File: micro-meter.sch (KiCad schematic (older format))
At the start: 105 parts, among them U1 XC6206P332MR, U2 STM32F411CEU6

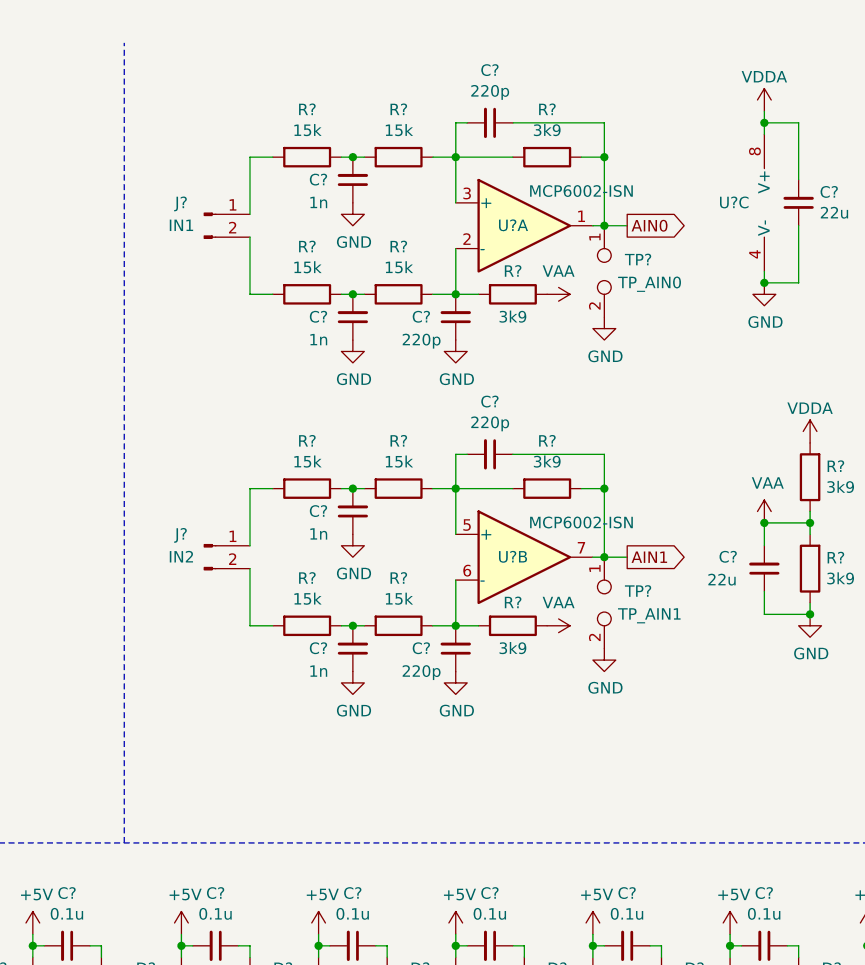
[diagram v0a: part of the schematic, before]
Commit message: Add MFB anti-alias filters
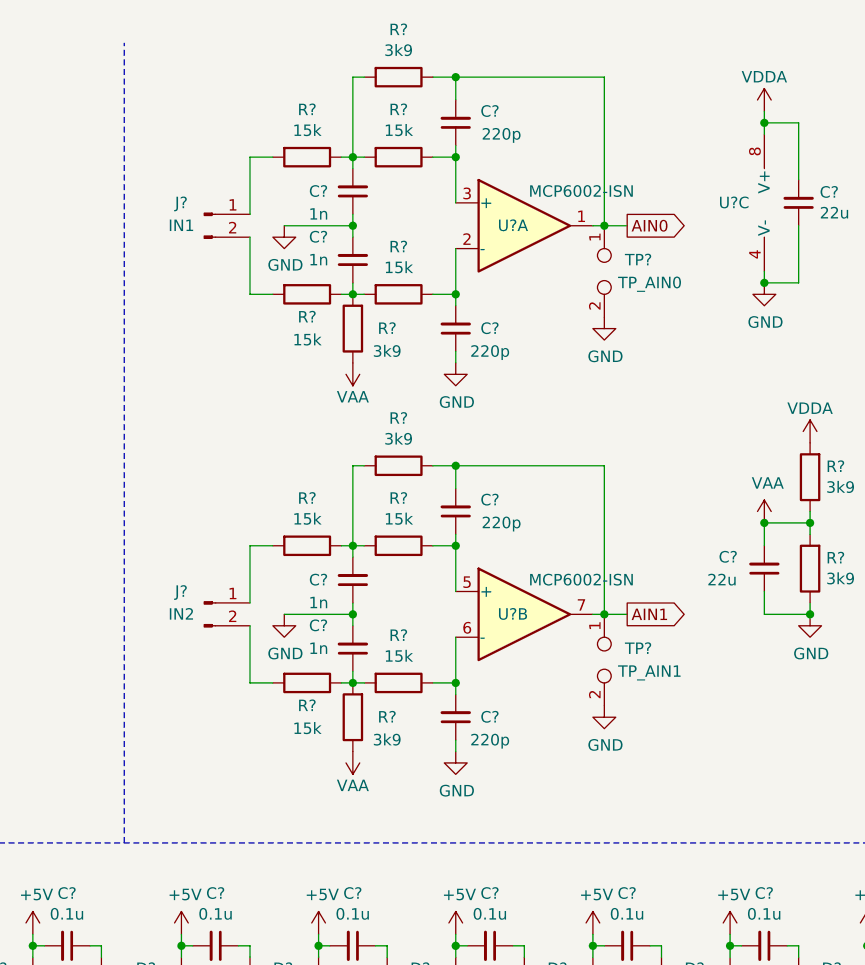
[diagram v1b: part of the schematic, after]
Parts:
- removed C? (x2): 220p, symbol Device:C_Small
- removed C? (x2): 1n, symbol Device:C_Small
- removed J?: IN2, symbol Connector:Conn_01x02_Male
- removed R? (x4): 15k, symbol Device:R
- removed R? (x2): 3k9, symbol Device:R
- removed TP?: TP_AIN1, symbol Connector:TestPoint_2Pole
- removed U?: MCP6002-ISN, symbol Amplifier_Operational:MCP6002-xSN
- added C? (x2): 220p, symbol Device:C_Small
- added C? (x2): 1n, symbol Device:C_Small
- added J?: IN2, symbol Connector:Conn_01x02_Male
- added R? (x4): 15k, symbol Device:R
- added R? (x2): 3k9, symbol Device:R
- added TP?: TP_AIN1, symbol Connector:TestPoint_2Pole
- added U?: MCP6002-ISN, symbol Amplifier_Operational:MCP6002-xSN
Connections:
- net AIN0: now also C?.2; no longer C?.1
- net AIN1: now also C?.2, R?.1, TP?.1, U?.7
- net GND: now also C?.2, C?.1, C?.1, C?.2, TP?.2; no longer C?.1
- net VAA: now also R?.1
- net at C?.2, R?.1, R?.2: now also R?.2
- net at R?.1, R?.2: now also C?.1, R?.2; no longer C?.2
- net at R?.1, U?.3 (+): now also C?.1; no longer C?.2, R?.2
- net at C?.2, R?.1, U?.2 (-): no longer R?.2
- new net: C?.2, R?.1, R?.2, R?.2
- new net: J?.1 (Pin_1), R?.2
- new net: C?.1, R?.1, R?.2, R?.2
- new net: J?.2 (Pin_2), R?.2
- new net: C?.1, R?.1, U?.5 (+)
- new net: C?.2, R?.1, U?.6 (-)
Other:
- moved on the sheet: C?, R?

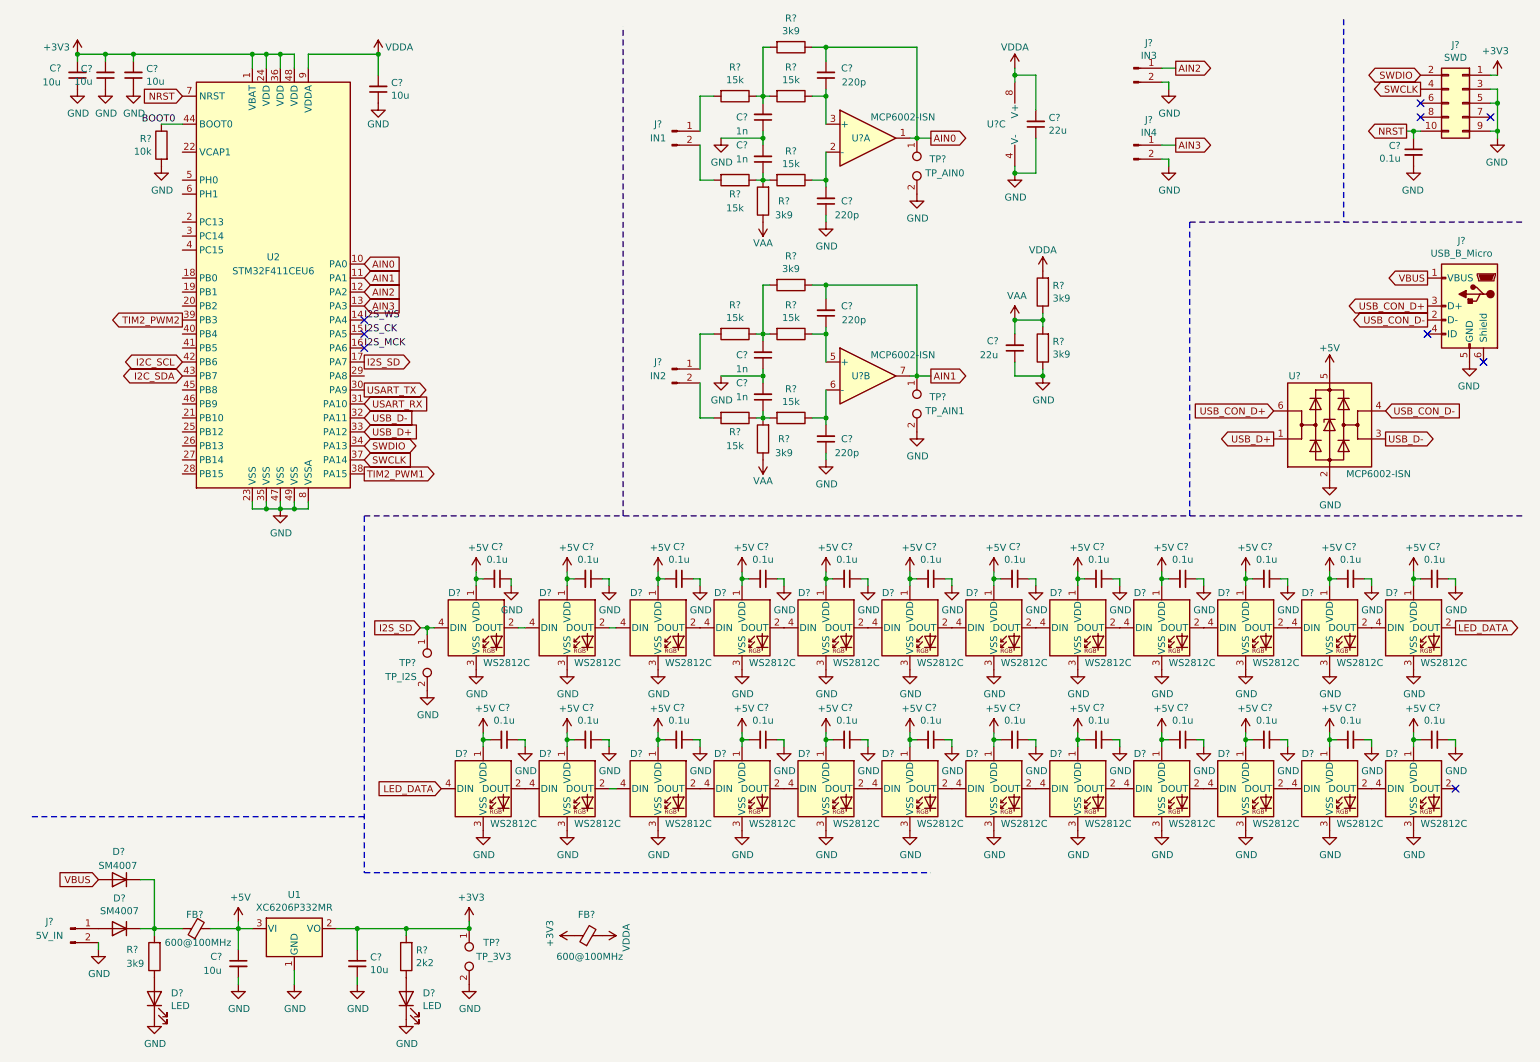
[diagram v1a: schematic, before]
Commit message: Cleanup schematics, add text
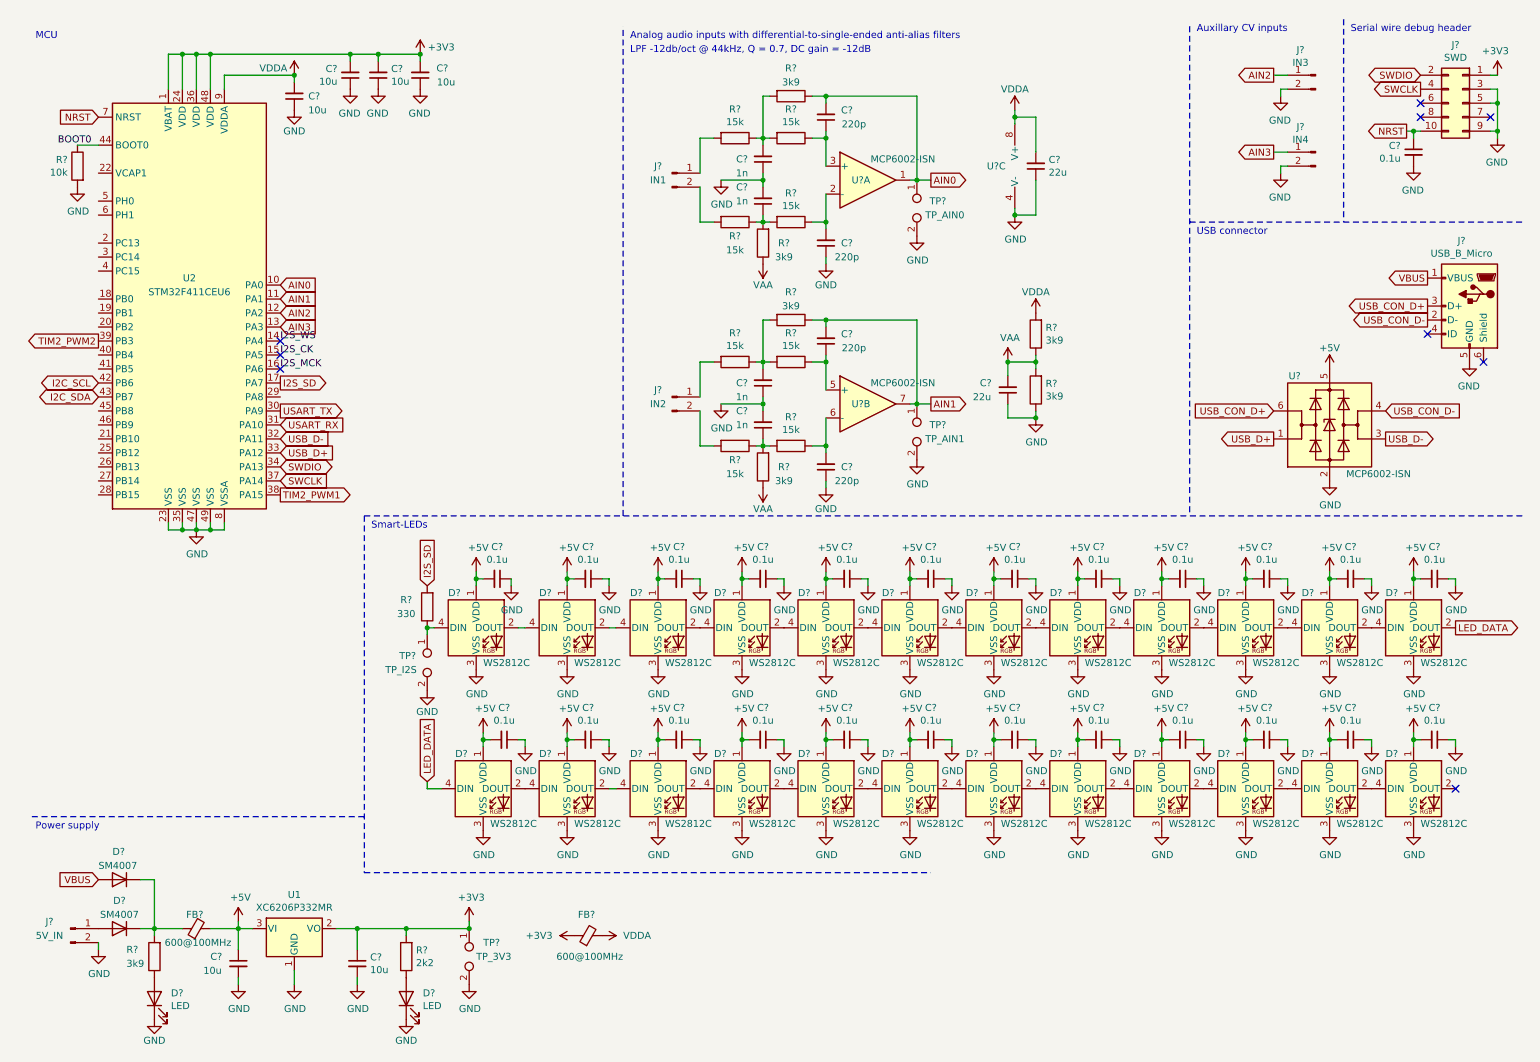
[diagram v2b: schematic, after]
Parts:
- added R?: 330, symbol Device:R
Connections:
- net I2S_SD: now also R?.2; no longer D?.4 (DIN), TP?.1
- new net: D?.4 (DIN), R?.1, TP?.1
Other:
- note added: "Analog audio inputs with differential-to-single-ended anti-alias filters"
- note added: "Auxillary CV inputs"
- note added: "LPF -12db/oct @ 44kHz, Q = 0.7, DC gain = -12dB"
- note added: "MCU"
- note added: "Power supply"
- note added: "Serial wire debug header"
- note added: "Smart-LEDs"
- note added: "USB connector"
- moved on the sheet: C?, J?, R?, TP?, U2, U?A, U?B, U?C

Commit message: Cleanup schematics
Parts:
- C?: value 10u -> 22u
- D? (x2): value LED -> GRN
- R?: value 10k -> 15k
- R?: value 330 -> 390
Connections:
- net at C?.1, R?.1: now also U?.2 (-); no longer U?.3 (+)
- net at C?.2, R?.1: now also U?.3 (+); no longer U?.2 (-)
- net at C?.1, R?.1: now also U?.6 (-); no longer U?.5 (+)
- net at C?.2, R?.1: now also U?.5 (+); no longer U?.6 (-)
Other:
- note added: "+4.3V"
- note added: "USB connector + ESD protection"
- note removed: "USB connector"
- moved on the sheet: C?, U?

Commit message: Cleanup schematics
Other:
- moved on the sheet: C?, FB?, R?, U?C

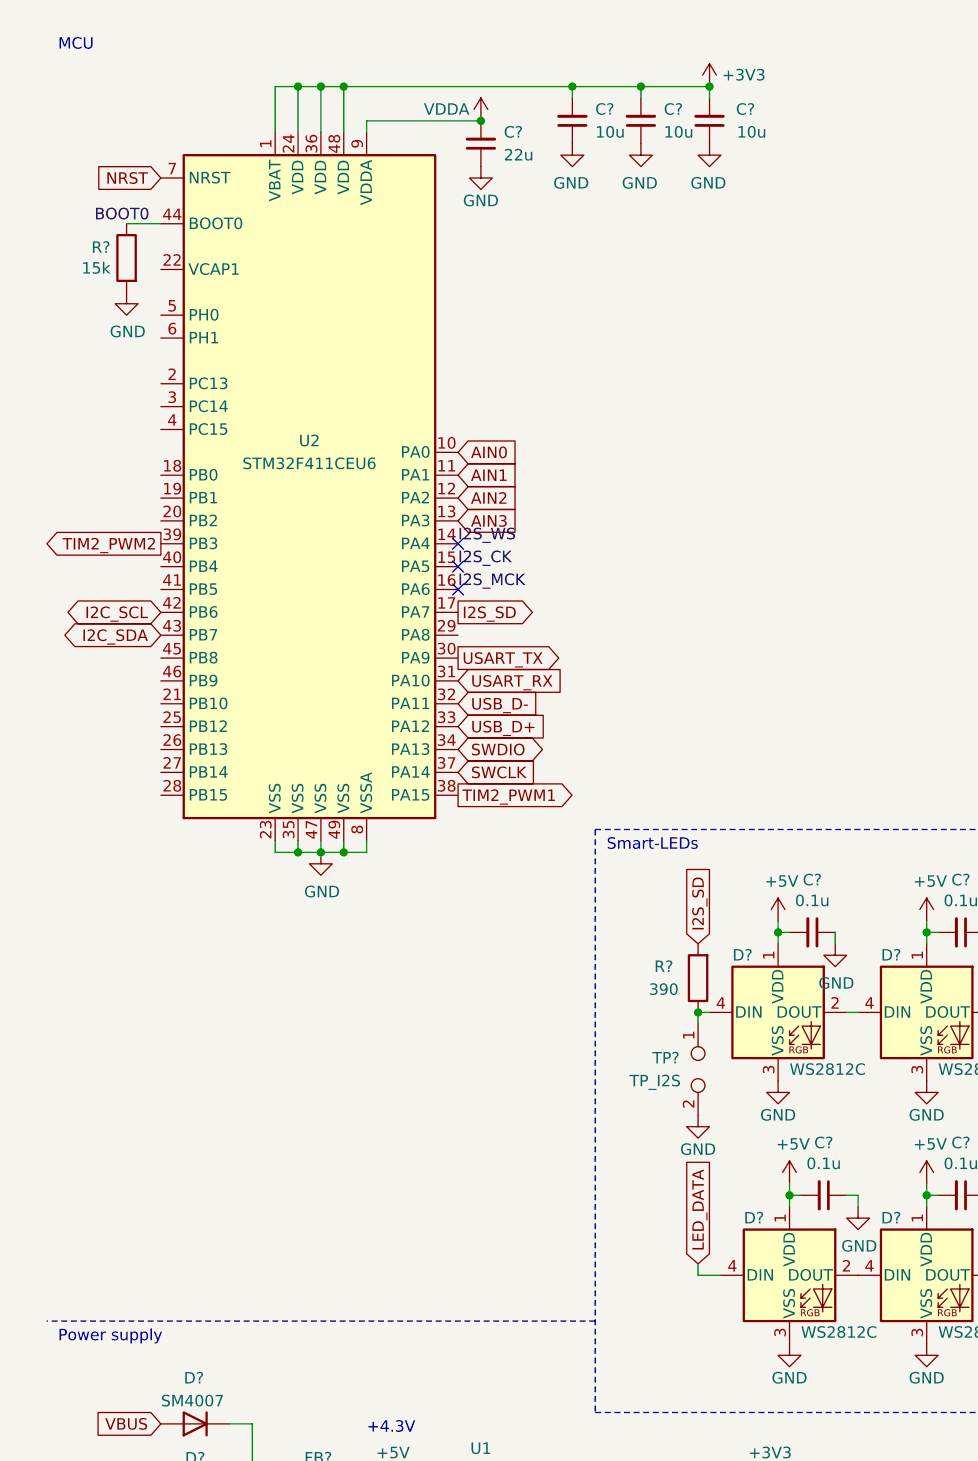
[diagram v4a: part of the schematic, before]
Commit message: Assign MCU pins
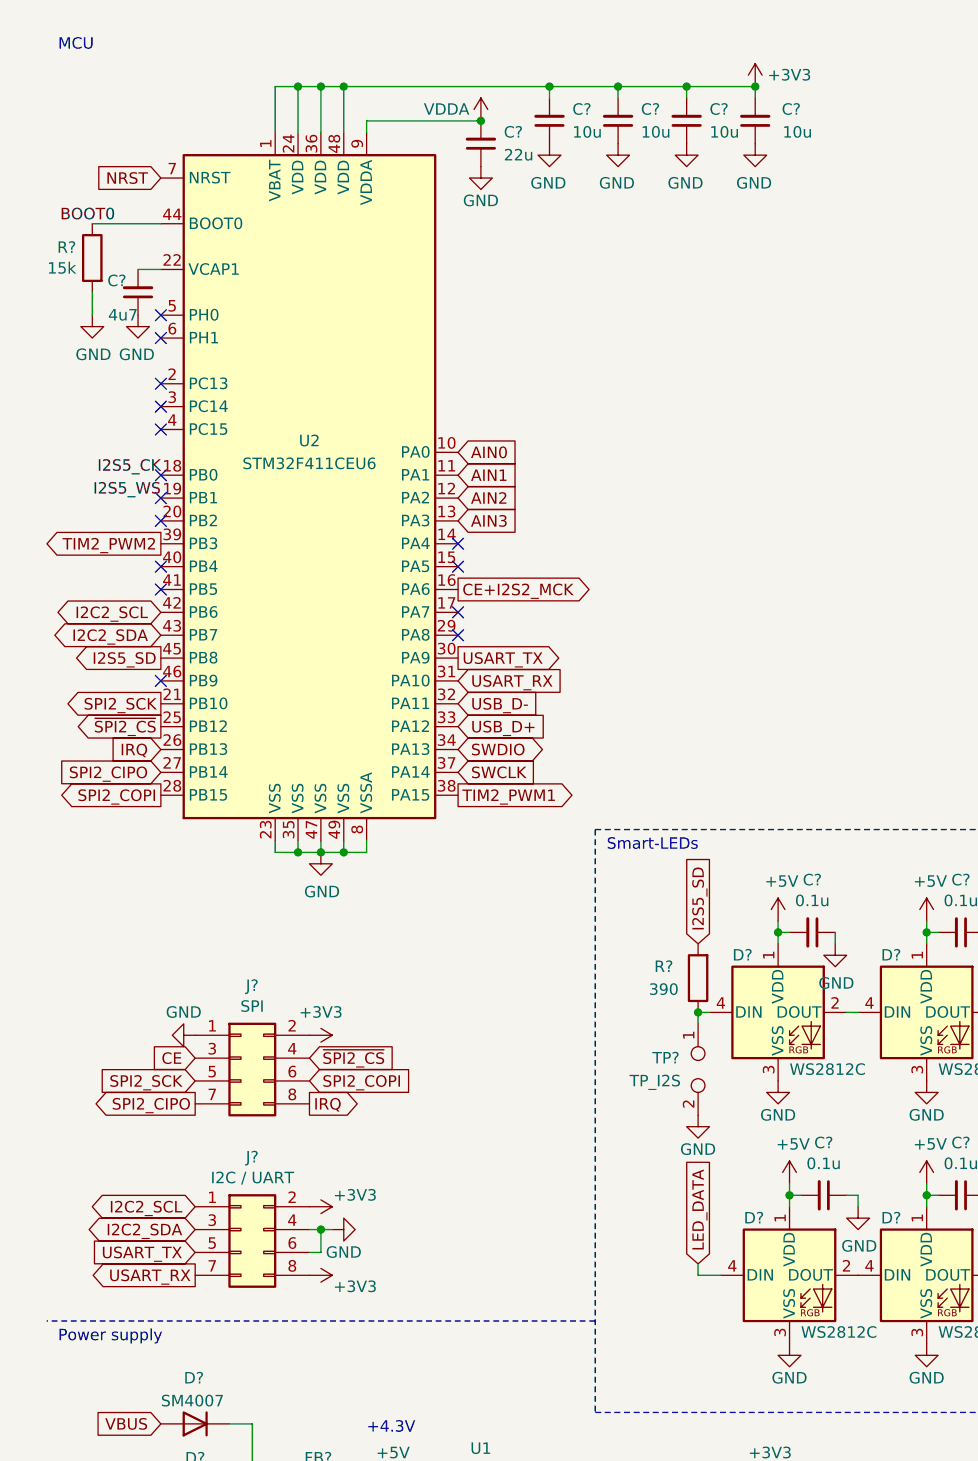
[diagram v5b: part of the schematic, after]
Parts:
- added C?: 4u7, symbol Device:C_Small
- added C?: 10u, symbol Device:C_Small
- added J?: SPI, symbol Connector_Generic:Conn_02x04_Odd_Even
- added J?: I2C / UART, symbol Connector_Generic:Conn_02x04_Odd_Even
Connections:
- net +3V3: now also C?.2, J?.2 (Pin_2), J?.2 (Pin_2), J?.8 (Pin_8)
- net GND: now also C?.1, C?.1, J?.1 (Pin_1), J?.4 (Pin_4), J?.6 (Pin_6)
- net USART_RX: now also J?.7 (Pin_7)
- net USART_TX: now also J?.5 (Pin_5)
- net I2S5_CK: now reaches U2.18 (PB0)
- net I2S5_WS: now reaches U2.19 (PB1)
- net SPI2_SCK: now reaches U2.21 (PB10)
- net SPI2_SCK: now also J?.5 (Pin_5)
- net at U2.22 (VCAP1): now also C?.2
- net ~SPI2_CS: now reaches U2.25 (PB12)
- net ~SPI2_CS: now also J?.4 (Pin_4)
- net IRQ: now reaches U2.26 (PB13)
- net IRQ: now also J?.8 (Pin_8)
- net SPI2_CIPO: now reaches U2.27 (PB14)
- net SPI2_CIPO: now also J?.7 (Pin_7)
- net SPI2_COPI: now reaches U2.28 (PB15)
- net SPI2_COPI: now also J?.6 (Pin_6)
- net I2S5_SD: now reaches U2.45 (PB8)
- net I2S5_SD: now also R?.2
- net I2C_SCL renamed I2C2_SCL
- net I2C2_SCL: now also J?.1 (Pin_1)
- net I2C_SDA renamed I2C2_SDA
- net I2C2_SDA: now also J?.3 (Pin_3)
- net I2S_CK: no longer names the net of U2.15 (PA5)
- net I2S_MCK renamed CE+I2S2_MCK
- net I2S_SD: no longer names the net of U2.17 (PA7)
- net I2S_SD: no longer R?.2
- net I2S_WS: no longer names the net of U2.14 (PA4)
- new net CE: J?.3 (Pin_3)
- no-connect marks 9 -> 21
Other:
- moved on the sheet: C?, R?

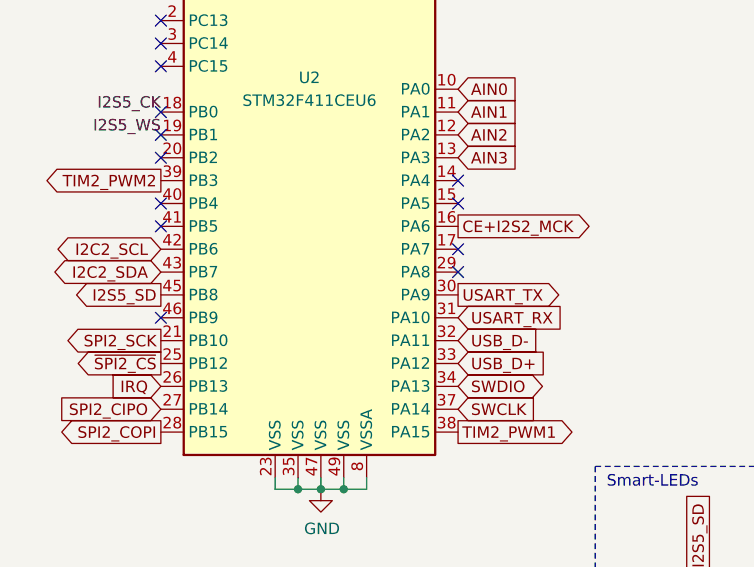
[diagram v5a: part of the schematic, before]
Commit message: Fix net labels
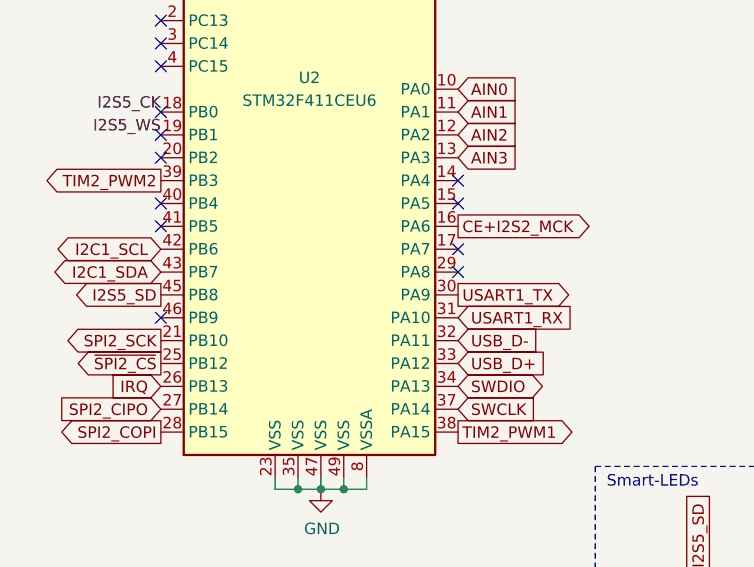
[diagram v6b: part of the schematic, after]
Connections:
- net I2C2_SCL: no longer U2.42 (PB6)
- net I2C2_SDA: no longer U2.43 (PB7)
- net USART_RX: no longer U2.31 (PA10)
- net USART_TX: no longer U2.30 (PA9)
- new net I2C1_SCL: U2.42 (PB6)
- new net I2C1_SDA: U2.43 (PB7)
- new net USART1_RX: U2.31 (PA10)
- new net USART1_TX: U2.30 (PA9)
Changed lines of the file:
@@
 $EndDescr
 Text GLabel 2300 3250 2    50   Output ~ 0
-USART_TX
+USART1_TX
 Text GLabel 2300 3350 2    50   Input ~ 0
-USART_RX
+USART1_RX
 Text GLabel 2300 2350 2    50   Input ~ 0
 AIN0
@@
 $EndComp
 Text GLabel 1000 3050 0    50   BiDi ~ 0
-I2C2_SCL
+I2C1_SCL
 Text GLabel 1000 3150 0    50   BiDi ~ 0
-I2C2_SDA
+I2C1_SDA
 $Comp
 L Connector:TestPoint_2Pole TP?
